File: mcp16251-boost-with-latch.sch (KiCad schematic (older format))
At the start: 39 parts, among them J1 THT_Castellated, J10 THT_Castellated, J11 SMD_pad, J12 THT_Castellated, J13 SMD_pad, J2 THT_Castellated, J3 THT_Castellated, J4 SMD_pad, J5 SMD_pad, J6 SMD_pad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

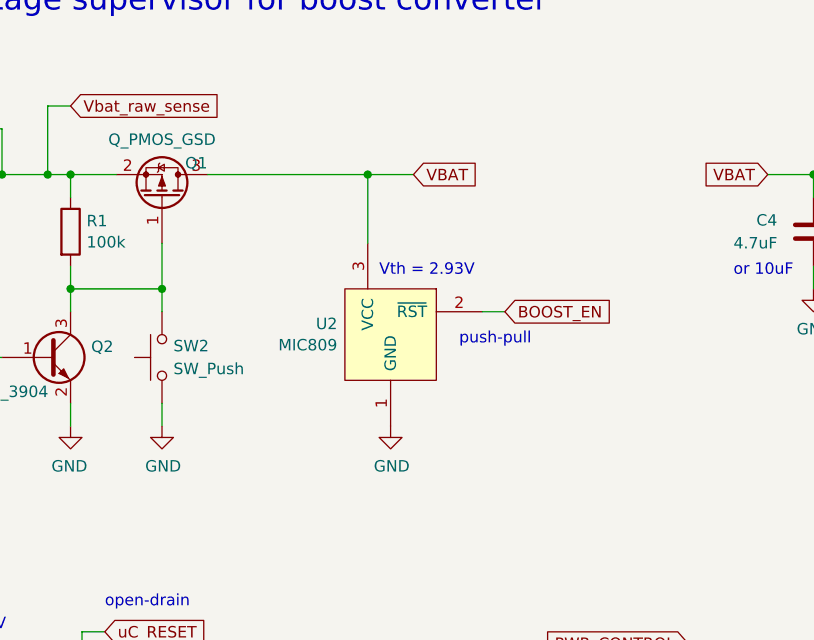
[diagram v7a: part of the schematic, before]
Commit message: Schematic tuning, footprint assignment, netlist.
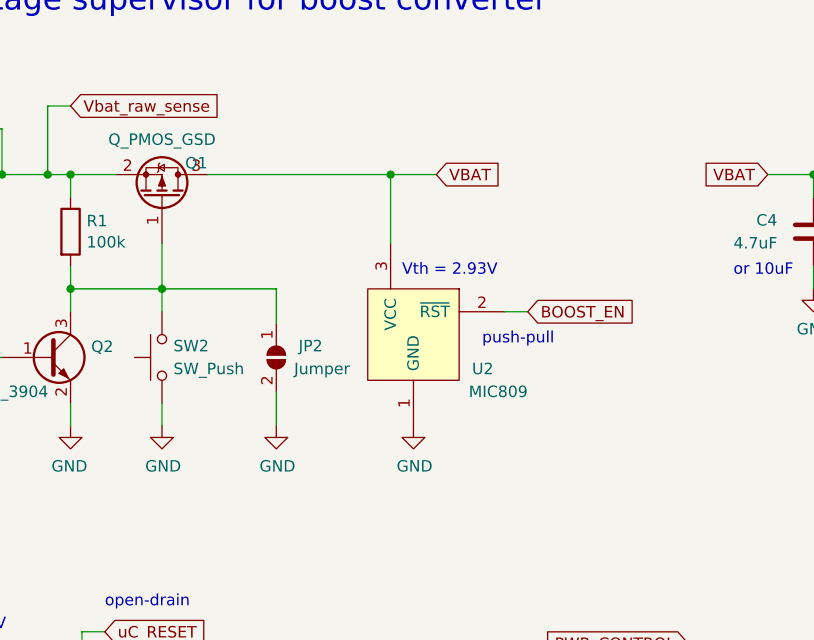
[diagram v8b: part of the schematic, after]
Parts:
- added JP2: Jumper, MCP16251_module:R_0805_HS, symbol Jumper:SolderJumper_2_Open
- F1: footprint (none) -> MCP16251_module:R_1206_HS
- Q3, Q4, U2, U3: footprint (none) -> MCP16251_module:SOT-23_HS
- U4: footprint (none) -> MCP16251_module:SOT-23-5_HS
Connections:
- net GND: now also JP2.2 (B)
- net at Q1.1 (G), Q2.3 (C), R1.2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: now also JP2.1 (A)
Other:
- moved on the sheet: U2
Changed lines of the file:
@@
 Text GLabel 1400 2750 0    50   Input ~ 0
 PWR_CONTROL
-Text GLabel 3700 1950 2    50   Input ~ 0
+Text GLabel 3800 1950 2    50   Input ~ 0
 VBAT
 Text Notes 1650 1250 0    100  ~ 0
@@
 L _Project_Local:MIC809 U2
 U 1 1 5C26A349
-P 3600 2750
-F 0 "U2" H 3367 2897 50  0000 R CNN
-F 1 "MIC809" H 3367 2804 50  0000 R CNN
-F 2 "" H 3600 2750 50  0001 C CNN
-F 3 "" H 3600 2750 50  0001 C CNN
-	1    3600 2750
+P 3700 2750
+F 0 "U2" H 4050 2700 50  0000 R CNN
+F 1 "MIC809" H 4200 2600 50  0000 R CNN
+F 2 "MCP16251_module:SOT-23_HS" H 3700 2750 50  0001 C CNN
+F 3 "" H 3700 2750 50  0001 C CNN
+	1    3700 2750
 	1    0    0    -1
 $EndComp
@@
 L power:GND #PWR0104
 U 1 1 5C26A716
-P 3600 3050
-F 0 "#PWR0104" H 3600 2800 50  0001 C CNN
-F 1 "GND" H 3605 2874 50  0000 C CNN
-F 2 "" H 3600 3050 50  0001 C CNN
-F 3 "" H 3600 3050 50  0001 C CNN
-	1    3600 3050
-	1    0    0    -1
-$EndComp
-Text GLabel 4100 2550 2    50   Input ~ 0
+P 3700 3050
+F 0 "#PWR0104" H 3700 2800 50  0001 C CNN
+F 1 "GND" H 3705 2874 50  0000 C CNN
+F 2 "" H 3700 3050 50  0001 C CNN
+F 3 "" H 3700 3050 50  0001 C CNN
+	1    3700 3050
+	1    0    0    -1
+$EndComp
+Text GLabel 4200 2550 2    50   Input ~ 0
 BOOST_EN
 Wire Wire Line
-	4000 2550 4100 2550
+	4100 2550 4200 2550
 Text GLabel 6050 2150 0    50   Input ~ 0
 BOOST_EN
-Text Notes 3550 2400 0    50   ~ 0
+Text Notes 3650 2400 0    50   ~ 0
 Vth = 2.93V
 $Comp
@@
 F 0 "F1" V 817 1900 50  0000 C CNN
 F 1 "Polyfuse" V 910 1900 50  0000 C CNN
-F 2 "" H 1100 1700 50  0001 L CNN
+F 2 "MCP16251_module:R_1206_HS" H 1100 1700 50  0001 L CNN
 F 3 "~" H 1050 1900 50  0001 C CNN
 	1    1050 1900
@@
 	2200 2950 2200 3050
 Wire Wire Line
-	2800 1950 3500 1950
-Wire Wire Line
-	3500 1950 3500 2250
-Connection ~ 3500 1950
-Wire Wire Line
-	3500 1950 3700 1950
+	3600 1950 3600 2250
+Connection ~ 3600 1950
+Wire Wire Line
+	3600 1950 3800 1950
 Wire Wire Line
 	5450 1950 5250 1950
@@
 F 0 "U3" H 1267 4447 50  0000 R CNN
 F 1 "MIC803" H 1267 4354 50  0000 R CNN
-F 2 "" H 1500 4300 50  0001 C CNN
+F 2 "MCP16251_module:SOT-23_HS" H 1500 4300 50  0001 C CNN
 F 3 "" H 1500 4300 50  0001 C CNN
 	1    1500 4300
@@
 F 0 "Q4" V 8146 3600 50  0000 C CNN
 F 1 "Q_PMOS_GSD" V 8053 3600 50  0000 C CNN
-F 2 "" H 8000 3700 50  0001 C CNN
+F 2 "MCP16251_module:SOT-23_HS" H 8000 3700 50  0001 C CNN
 F 3 "~" H 7800 3600 50  0001 C CNN
 	1    7800 3600
@@
 F 0 "Q3" V 7446 3600 50  0000 C CNN
 F 1 "Q_PMOS_GSD" V 7353 3600 50  0000 C CNN
-F 2 "" H 7300 3700 50  0001 C CNN
+F 2 "MCP16251_module:SOT-23_HS" H 7300 3700 50  0001 C CNN
 F 3 "~" H 7100 3600 50  0001 C CNN
 	1    7100 3600
@@
 Text GLabel 9400 3300 2    50   Input ~ 0
 uC_ADC
-Text Notes 3900 2700 0    50   ~ 0
+Text Notes 4000 2700 0    50   ~ 0
 push-pull
 $Comp
@@
 F 0 "U4" H 7800 4150 50  0000 C CNN
 F 1 "MIC2777" H 7700 4050 50  0000 C CNN
-F 2 "" H 8100 4300 50  0001 C CNN
+F 2 "MCP16251_module:SOT-23-5_HS" H 8100 4300 50  0001 C CNN
 F 3 "" H 8100 4300 50  0001 C CNN
 	1    8100 4300
@@
 	2250 4100 2250 3950
 Connection ~ 2250 4100
+$Comp
+L Jumper:SolderJumper_2_Open JP2
+U 1 1 5C6B91A1
+P 3100 2750
+F 0 "JP2" V 3050 2900 50  0000 C CNN
+F 1 "Jumper" V 3150 2950 50  0000 C CNN
+F 2 "MCP16251_module:R_0805_HS" H 3100 2750 50  0001 C CNN
+F 3 "~" H 3100 2750 50  0001 C CNN
+	1    3100 2750
+	0    1    1    0
+$EndComp
+Wire Wire Line
+	2800 1950 3600 1950
+Wire Wire Line
+	2600 2450 3100 2450
+Wire Wire Line
+	3100 2450 3100 2600
+Wire Wire Line
+	3100 2900 3100 3050
+$Comp
+L power:GND #PWR0107
+U 1 1 5C6C4B3B
+P 3100 3050
+F 0 "#PWR0107" H 3100 2800 50  0001 C CNN
+F 1 "GND" H 3105 2874 50  0000 C CNN
+F 2 "" H 3100 3050 50  0001 C CNN
+F 3 "" H 3100 3050 50  0001 C CNN
+	1    3100 3050
+	1    0    0    -1
+$EndComp
 $EndSCHEMATC
